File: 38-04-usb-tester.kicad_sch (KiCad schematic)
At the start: 64 parts, among them J1 Conn_1x05, J2 USB_C_12401832E402A, J3 USB_C_12401832E402A, J4 USB_Micro-B_KH-MICRO5P-JN, J5 USB_Mini-B_U-M-M5DD-W-1, J6 USB3_A_HC-USB3.0-L168-WP, SW1 SW_DPDT_x2, SW2 ZX-1.27BM-4PSMD, U1 STM32C031K6Tx

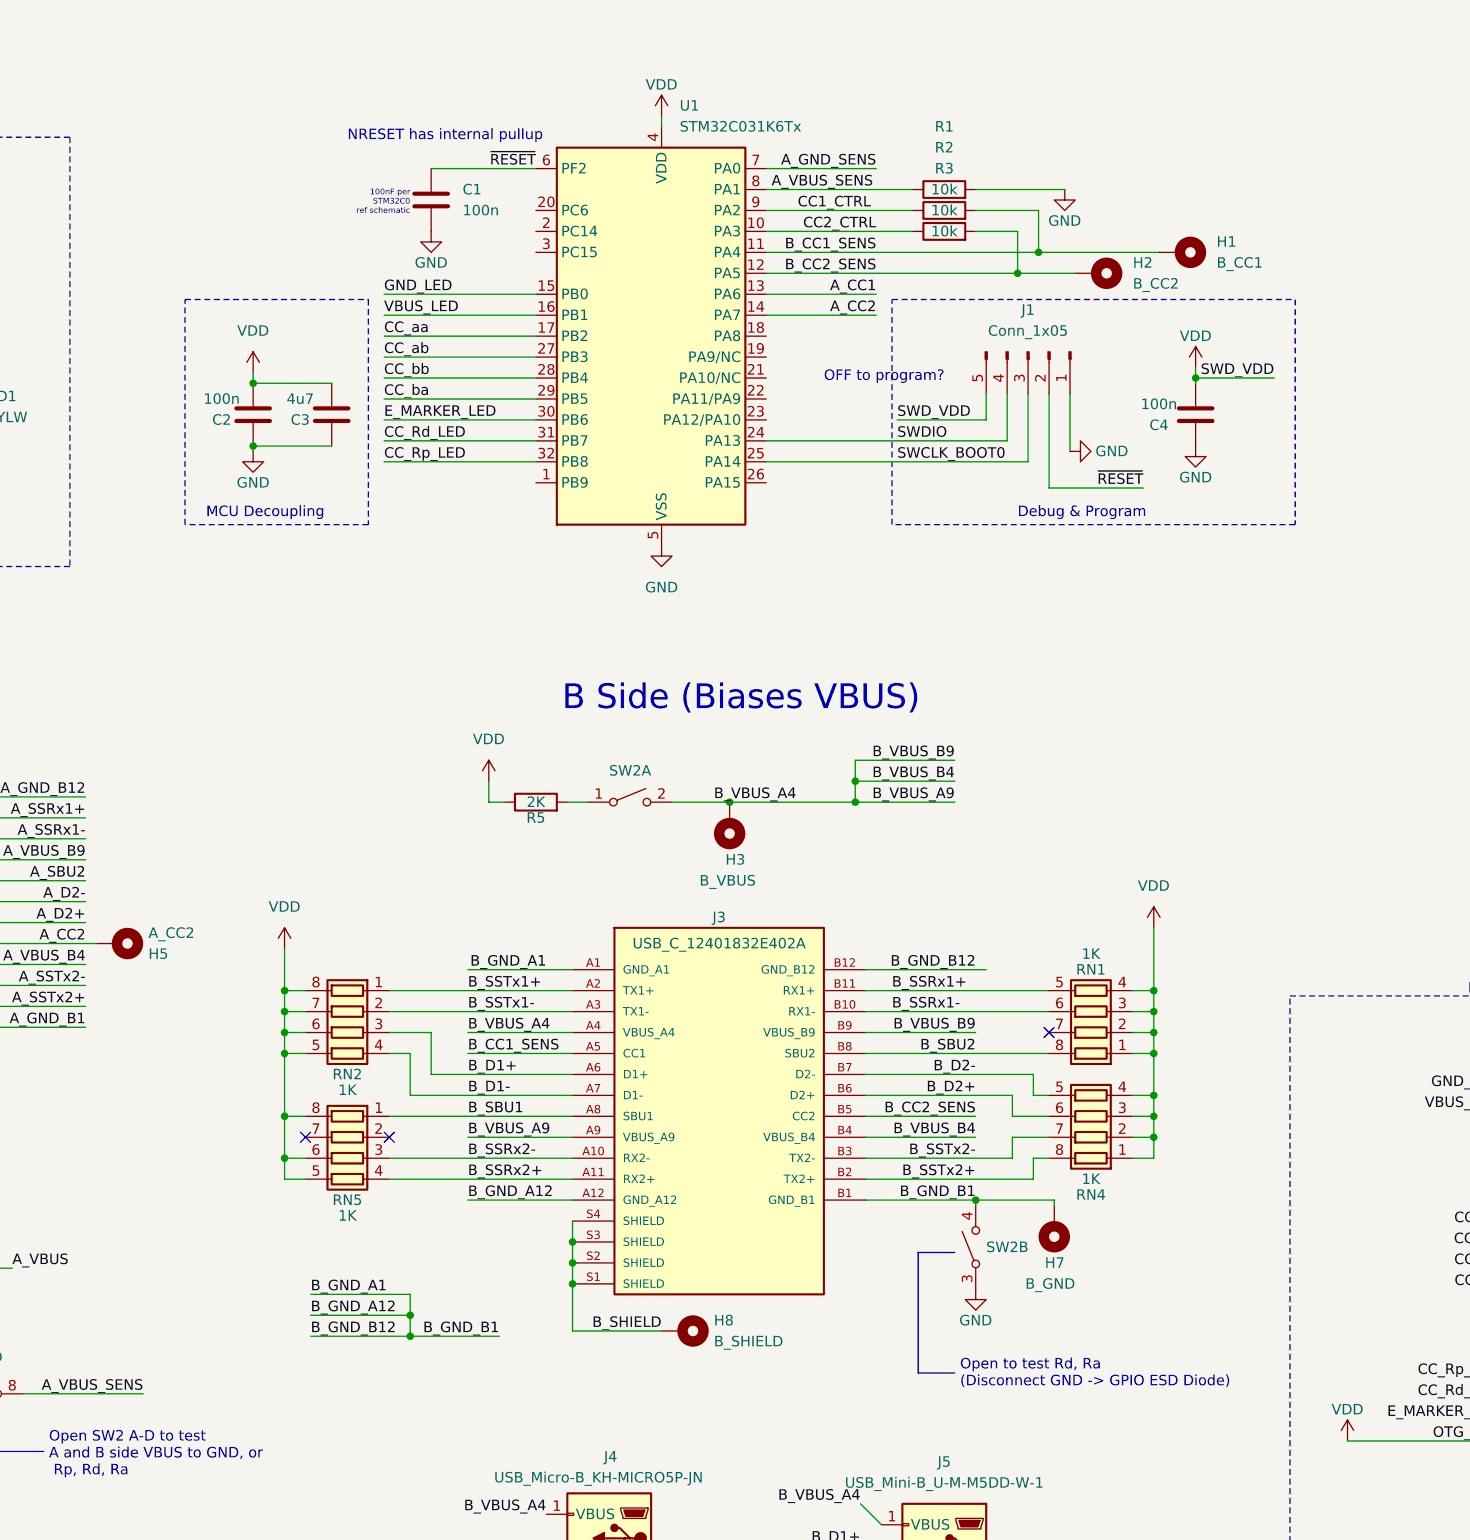
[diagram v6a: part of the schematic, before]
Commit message: renamed user symbol file
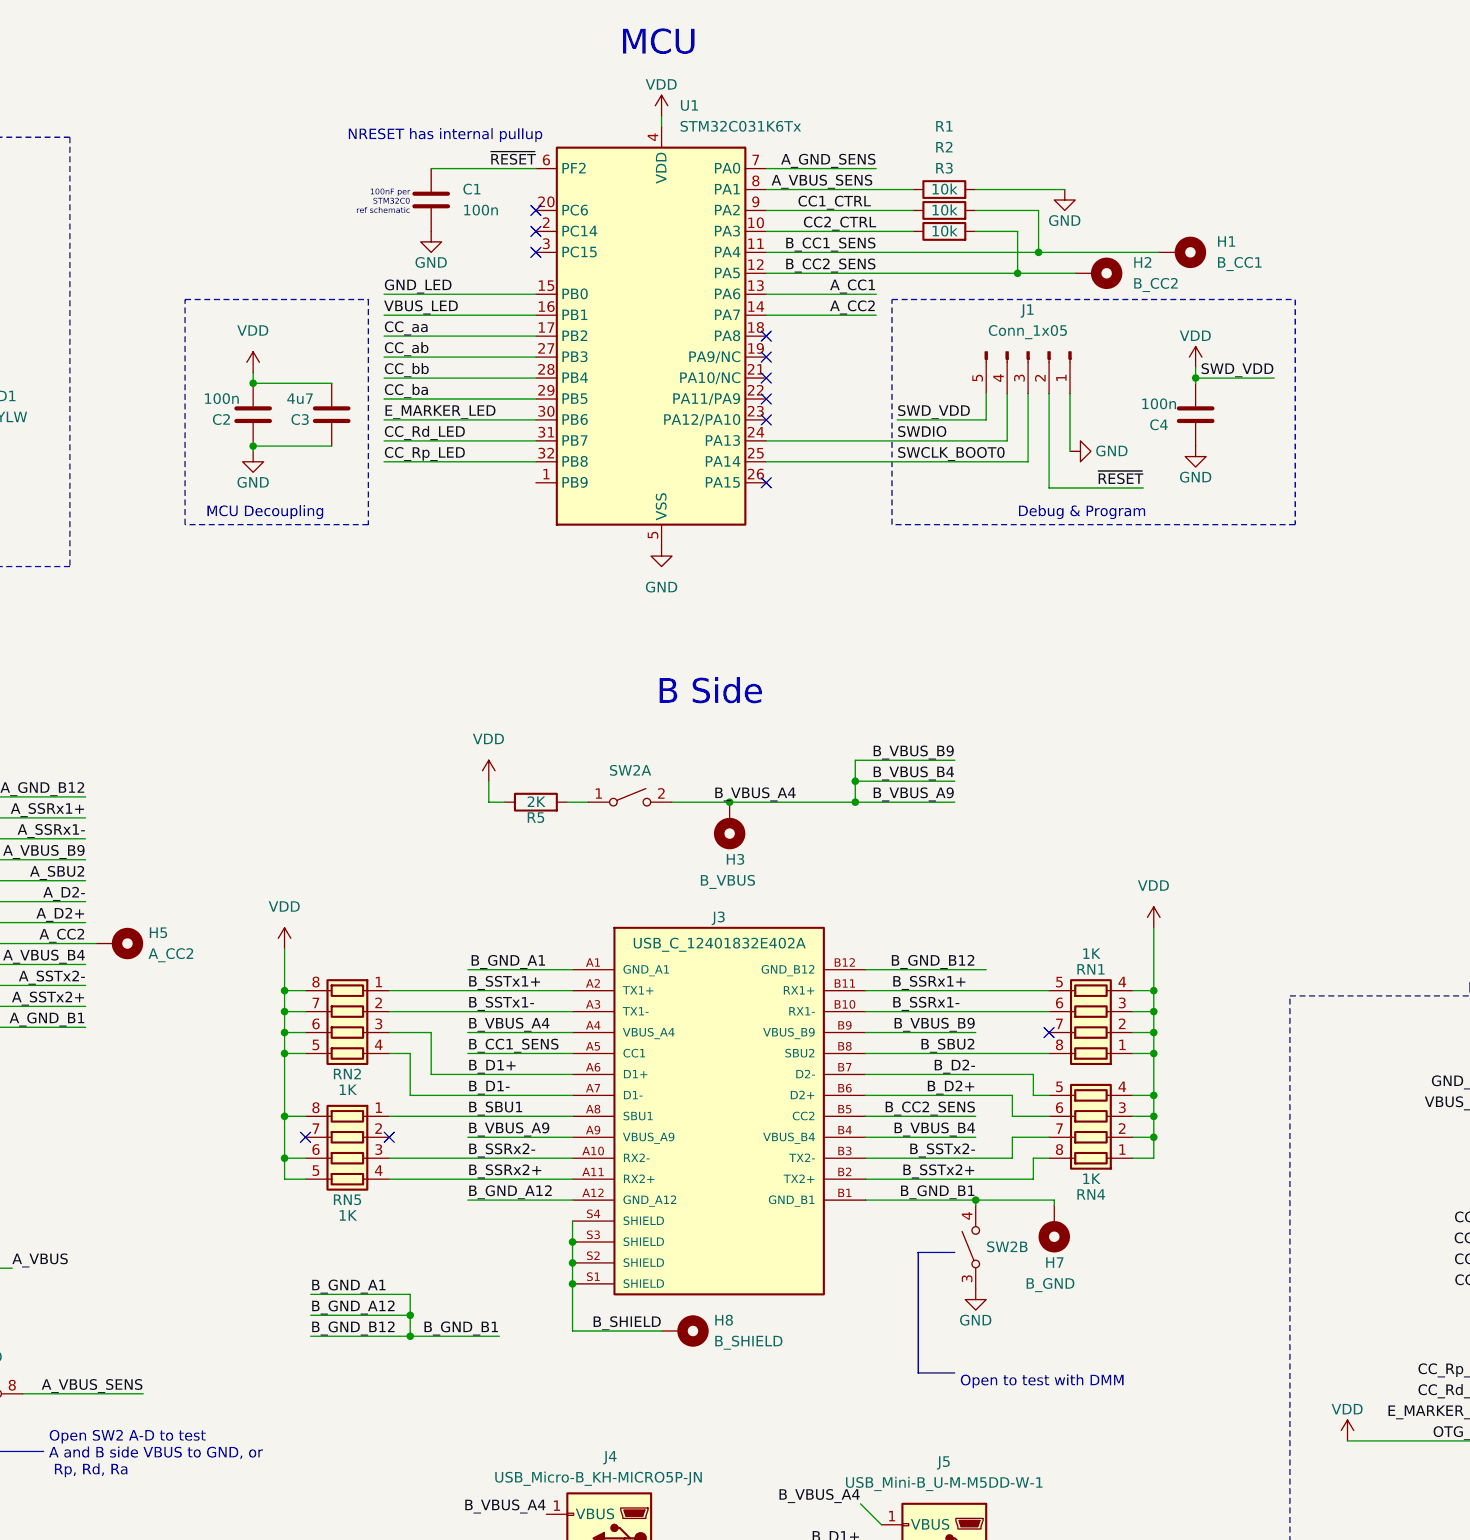
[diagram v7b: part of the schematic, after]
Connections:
- no-connect marks 9 -> 18
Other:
- note added: "B Side"
- note added: "MCU"
- note added: "Open to test with DMM"
- note removed: "B Side (Biases VBUS)"
- note removed: "OFF to program?"
- note removed: "Open to test Rd, Ra (Disconnect GND -> GPIO ESD Diode)"
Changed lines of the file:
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@@
   (junction (at 367.03 144.145) (diameter 0) (color 0 0 0 0)
   )
+  (no_connect (at 171.45 70.485))
   (no_connect (at 55.245 45.72))
+  (no_connect (at 143.51 40.005))
+  (no_connect (at 171.45 60.325))
+  (no_connect (at 171.45 62.865))
+  (no_connect (at 171.45 57.785))
   (no_connect (at 270.51 149.225))
   (no_connect (at 270.51 151.765))
   (no_connect (at 260.35 151.765))
+  (no_connect (at 143.51 37.465))
   (no_connect (at 260.35 149.225))
+  (no_connect (at 143.51 42.545))
+  (no_connect (at 171.45 52.705))
   (no_connect (at 46.355 45.72))
   (no_connect (at 115.57 149.86))
   (no_connect (at 125.73 149.86))
+  (no_connect (at 171.45 55.245))
   (no_connect (at 205.74 137.16))
   (wire (pts (xy 74.93 160.655) (xy 74.93 163.195))
@@
     (effects (font (size 1.27 1.27)) (justify left bottom))
   )
+  (text "MCU" (at 153.67 19.05 0)
+    (effects (font (size 3 3)) (justify left bottom))
+  )
   (text "100nF per \nSTM32C0 \nref schematic" (at 128.27 38.1 0)
     (effects (font (size 0.7 0.7)) (justify right bottom))
@@
     (effects (font (size 1.27 1.27)) (justify left bottom))
   )
-  (text "OFF to program? " (at 178.435 58.42 0)
-    (effects (font (size 1.27 1.27)) (justify left bottom))
-  )
   (text "Power" (at 52.705 26.67 0)
     (effects (font (size 1.27 1.27)) (justify left bottom))
@@
     (effects (font (size 1.27 1.27)) (justify left bottom))
   )
-  (text "Open to test Rd, Ra\n(Disconnect GND -> GPIO ESD Diode)"
-    (at 194.945 180.34 0)
+  (text "Open to test with DMM" (at 194.945 180.34 0)
     (effects (font (size 1.27 1.27)) (justify left bottom))
   )
@@
     (effects (font (size 1.27 1.27)) (justify left bottom))
   )
-  (text "B Side (Biases VBUS)" (at 146.685 98.425 0)
+  (text "B Side" (at 158.115 97.79 0)
     (effects (font (size 3 3)) (justify left bottom))
   )
@@
   (symbol (lib_id "Mechanical:MountingHole_Pad") (at 92.71 126.365 270) (mirror x) (unit 1)
     (in_bom yes) (on_board yes) (dnp no)
-    (property "Reference" "H5" (at 96.52 127.635 90)
+    (property "Reference" "H5" (at 96.52 125.095 90)
       (effects (font (size 1.27 1.27)) (justify left))
     )
-    (property "Value" "A_CC2" (at 96.52 125.095 90)
+    (property "Value" "A_CC2" (at 96.52 127.635 90)
       (effects (font (size 1.27 1.27)) (justify left))
     )

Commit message: renamed libraries
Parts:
- H1, H10, H2, H3, H4, H5, H7, H9: footprint 01-UserLibary:Connector_Pad_Edge_Oval_5mm_Extended -> 01-UserFootprints:Connector_Pad_Edge_Oval_5mm_Extended
- J2, J3: footprint 01-UserLibary:USB_C_Receptacle_Amphenol_12401832E402A -> 01-UserFootprints:USB_C_Receptacle_Amphenol_12401832E402A
- J4: footprint 01-UserLibary:USB_Micro-B_Kinghelm-KH-MICRO5P-JN -> 01-UserFootprints:USB_Micro-B_Kinghelm-KH-MICRO5P-JN
- J5: footprint 01-UserLibary:USB_Mini-B_Korean-Hroparts_U-M-M5DD-W-1_SMD-5-4MP -> 01-UserFootprints:USB_Mini-B_Korean-Hroparts_U-M-M5DD-W-1_SMD-5-4MP
- J6: footprint 01-UserLibary:USB3_A_Hong-Cheng_HC-USB3.0-L168-WP_THT-9-2MP_P2.0mm -> 01-UserFootprints:USB3_A_Hong-Cheng_HC-USB3.0-L168-WP_THT-9-2MP_P2.0mm
- SW2: footprint 01-UserLibary:SW-DIP-4P_P1.27mm_SMD-2x4 -> 01-UserFootprints:SW-DIP-4P_P1.27mm_SMD-2x4
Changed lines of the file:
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@@
       (effects (font (size 1.27 1.27)) (justify left))
     )
-    (property "Footprint" "01-UserLibary:Connector_Pad_Edge_Oval_5mm_Extended" (at 206.375 160.655 0)
+    (property "Footprint" "01-UserFootprints:Connector_Pad_Edge_Oval_5mm_Extended" (at 206.375 160.655 0)
       (effects (font (size 1.27 1.27)) hide)
     )
@@
       (effects (font (size 1.27 1.27)) hide)
     )
-    (property "Footprint" "01-UserLibary:SW-DIP-4P_P1.27mm_SMD-2x4" (at 196.85 163.195 0)
+    (property "Footprint" "01-UserFootprints:SW-DIP-4P_P1.27mm_SMD-2x4" (at 196.85 163.195 0)
       (effects (font (size 1.27 1.27)) hide)
     )
@@
       (effects (font (size 1.27 1.27)) (justify right))
     )
-    (property "Footprint" "01-UserLibary:USB_Micro-B_Kinghelm-KH-MICRO5P-JN" (at 148.59 201.93 0)
+    (property "Footprint" "01-UserFootprints:USB_Micro-B_Kinghelm-KH-MICRO5P-JN" (at 148.59 201.93 0)
       (effects (font (size 1.27 1.27)) hide)
     )
@@
       (effects (font (size 1.27 1.27)))
     )
-    (property "Footprint" "01-UserLibary:Connector_Pad_Edge_Oval_5mm_Extended" (at 23.495 118.745 0)
+    (property "Footprint" "01-UserFootprints:Connector_Pad_Edge_Oval_5mm_Extended" (at 23.495 118.745 0)
       (effects (font (size 1.27 1.27)) hide)
     )
@@
       (effects (font (size 1.27 1.27)) (justify left))
     )
-    (property "Footprint" "01-UserLibary:Connector_Pad_Edge_Oval_5mm_Extended" (at 71.12 185.42 0)
+    (property "Footprint" "01-UserFootprints:Connector_Pad_Edge_Oval_5mm_Extended" (at 71.12 185.42 0)
       (effects (font (size 1.27 1.27)) hide)
     )
@@
       (effects (font (size 1.27 1.27)) (justify right))
     )
-    (property "Footprint" "01-UserLibary:USB3_A_Hong-Cheng_HC-USB3.0-L168-WP_THT-9-2MP_P2.0mm" (at 52.07 211.455 0)
+    (property "Footprint" "01-UserFootprints:USB3_A_Hong-Cheng_HC-USB3.0-L168-WP_THT-9-2MP_P2.0mm" (at 52.07 211.455 0)
       (effects (font (size 1.27 1.27)) hide)
     )
@@
       (effects (font (size 1.27 1.27)) (justify left))
     )
-    (property "Footprint" "01-UserLibary:Connector_Pad_Edge_Oval_5mm_Extended" (at 211.455 45.085 0)
+    (property "Footprint" "01-UserFootprints:Connector_Pad_Edge_Oval_5mm_Extended" (at 211.455 45.085 0)
       (effects (font (size 1.27 1.27)) hide)
     )
@@
       (effects (font (size 1.27 1.27)) (justify left))
     )
-    (property "Footprint" "01-UserLibary:Connector_Pad_Edge_Oval_5mm_Extended" (at 167.005 111.76 0)
+    (property "Footprint" "01-UserFootprints:Connector_Pad_Edge_Oval_5mm_Extended" (at 167.005 111.76 0)
       (effects (font (size 1.27 1.27)) hide)
     )
@@
       (effects (font (size 1.27 1.27)))
     )
-    (property "Footprint" "01-UserLibary:USB_C_Receptacle_Amphenol_12401832E402A" (at 165.735 144.78 0)
+    (property "Footprint" "01-UserFootprints:USB_C_Receptacle_Amphenol_12401832E402A" (at 165.735 144.78 0)
       (effects (font (size 1.27 1.27)) (justify bottom) hide)
     )
@@
       (effects (font (size 1.27 1.27)) (justify left))
     )
-    (property "Footprint" "01-UserLibary:Connector_Pad_Edge_Oval_5mm_Extended" (at 221.615 42.545 0)
+    (property "Footprint" "01-UserFootprints:Connector_Pad_Edge_Oval_5mm_Extended" (at 221.615 42.545 0)
       (effects (font (size 1.27 1.27)) hide)
     )
@@
       (effects (font (size 1.27 1.27)) hide)
     )
-    (property "Footprint" "01-UserLibary:SW-DIP-4P_P1.27mm_SMD-2x4" (at 76.2 180.975 0)
+    (property "Footprint" "01-UserFootprints:SW-DIP-4P_P1.27mm_SMD-2x4" (at 76.2 180.975 0)
       (effects (font (size 1.27 1.27)) hide)
     )
@@
       (effects (font (size 1.27 1.27)) hide)
     )
-    (property "Footprint" "01-UserLibary:SW-DIP-4P_P1.27mm_SMD-2x4" (at 154.94 109.22 0)
+    (property "Footprint" "01-UserFootprints:SW-DIP-4P_P1.27mm_SMD-2x4" (at 154.94 109.22 0)
       (effects (font (size 1.27 1.27)) hide)
     )
@@
       (effects (font (size 1.27 1.27)) hide)
     )
-    (property "Footprint" "01-UserLibary:SW-DIP-4P_P1.27mm_SMD-2x4" (at 38.1 180.975 0)
+    (property "Footprint" "01-UserFootprints:SW-DIP-4P_P1.27mm_SMD-2x4" (at 38.1 180.975 0)
       (effects (font (size 1.27 1.27)) hide)
     )
@@
       (effects (font (size 1.27 1.27)))
     )
-    (property "Footprint" "01-UserLibary:USB_Mini-B_Korean-Hroparts_U-M-M5DD-W-1_SMD-5-4MP" (at 189.23 203.2 0)
+    (property "Footprint" "01-UserFootprints:USB_Mini-B_Korean-Hroparts_U-M-M5DD-W-1_SMD-5-4MP" (at 189.23 203.2 0)
       (effects (font (size 1.27 1.27)) hide)
     )
@@
       (effects (font (size 1.27 1.27)) (justify left))
     )
-    (property "Footprint" "01-UserLibary:Connector_Pad_Edge_Oval_5mm_Extended" (at 31.75 185.42 0)
+    (property "Footprint" "01-UserFootprints:Connector_Pad_Edge_Oval_5mm_Extended" (at 31.75 185.42 0)
       (effects (font (size 1.27 1.27)) hide)
     )
@@
       (effects (font (size 1.27 1.27)) (justify left))
     )
-    (property "Footprint" "01-UserLibary:Connector_Pad_Edge_Oval_5mm_Extended" (at 92.71 126.365 0)
+    (property "Footprint" "01-UserFootprints:Connector_Pad_Edge_Oval_5mm_Extended" (at 92.71 126.365 0)
       (effects (font (size 1.27 1.27)) hide)
     )
@@
       (effects (font (size 1.27 1.27)))
     )
-    (property "Footprint" "01-UserLibary:USB_C_Receptacle_Amphenol_12401832E402A" (at 59.055 123.825 0)
+    (property "Footprint" "01-UserFootprints:USB_C_Receptacle_Amphenol_12401832E402A" (at 59.055 123.825 0)
       (effects (font (size 1.27 1.27)) (justify bottom) hide)
     )
